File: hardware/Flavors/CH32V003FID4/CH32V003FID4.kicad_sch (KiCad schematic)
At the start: 22 parts, among them U1 TPS92520QDAPRQ1, U3 CH32V003F4P6

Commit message: Syncing the latest update on KiCAD (these updates are going to be randomly pushed i am not using Git for tracking it) and probably stuff will be without meaningfull commits. Commits are mainly for the code progress (and whatever that catches on KiCAD)
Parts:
- removed D1, D2: D_Shockley, Diode_SMD:D_SMA, symbol Device:D_Shockley
- added C12: 0.47u, Capacitor_SMD:C_1206_3216Metric, symbol Device:C_Small
- added C13: 47 µ, symbol Device:C_Polarized
- added D1, D2: 100V, symbol Device:D_Schottky
- added D3: SMBJ48A, symbol Device:D_TVS
- added J1: 48 POWER IN, symbol Connector:Screw_Terminal_01x02
- added L2: 150 u, symbol Device:L_Small
- added R4: 4.7K, symbol Device:R_Small
- added R5: 10K, symbol Device:R_Small
- added R6: 4.7 k (place holder), symbol Device:R_Small
- C10: value C_Small -> 100n
- C11: value C_Small -> 0.47u
- C4, C5: value C -> 1u
- C7, C8: value C_Small -> 2.2u
- C9: value C_Small -> 4.7u
- L1: value L_Small -> 150 u
- R1: value R_Small -> 10
- R2, R3: value R_Small -> 0.33
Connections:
- net +5V: now also C9.2, U1.9 (V5D), R4.1, R5.1; no longer C10.2, U1.8 (V5A)
- net GND: now also C10.2, C9.1, U1.33 (EP), C13.2, D1.2 (A), D2.2 (A), D3.1 (A1), J1.1 (Pin_1), R6.1; no longer C10.1, C9.2
- net VLED1: now also D2.1 (K)
- net VLED2: now also D1.1 (K)
- net at R2.1, U1.18 (CSP1): now also L2.1
- net at U1.19 (BST1): now also C12.1
- net at U1.20 (SW1): now also U1.21 (SW1), C12.2, L2.2
- net !FLT: now reaches U1.22 (FLT#)
- net !FLT: now also R5.2
- net at U1.23 (LHI): now also R6.2
- net SSN: now reaches U1.24 (SSN)
- net SCK: now reaches U1.25 (SCK)
- net MISO: now reaches U1.26 (MISO)
- net MISO: now also R4.2
- net MOSI: now reaches U1.27 (MOSI)
- net at C11.2, U1.28 (SW2), U1.29 (SW2): now also L1.2
- net at R3.1, U1.31 (CSP2): now also L1.1
- net VBOOST renamed +48V
- net +48V: now also C13.1, D3.2 (A2), J1.2 (Pin_2)
- new net: C10.1, R1.1, U1.8 (V5A)
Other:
- note added: "Inputs"
- moved on the sheet: C10, C5, L1

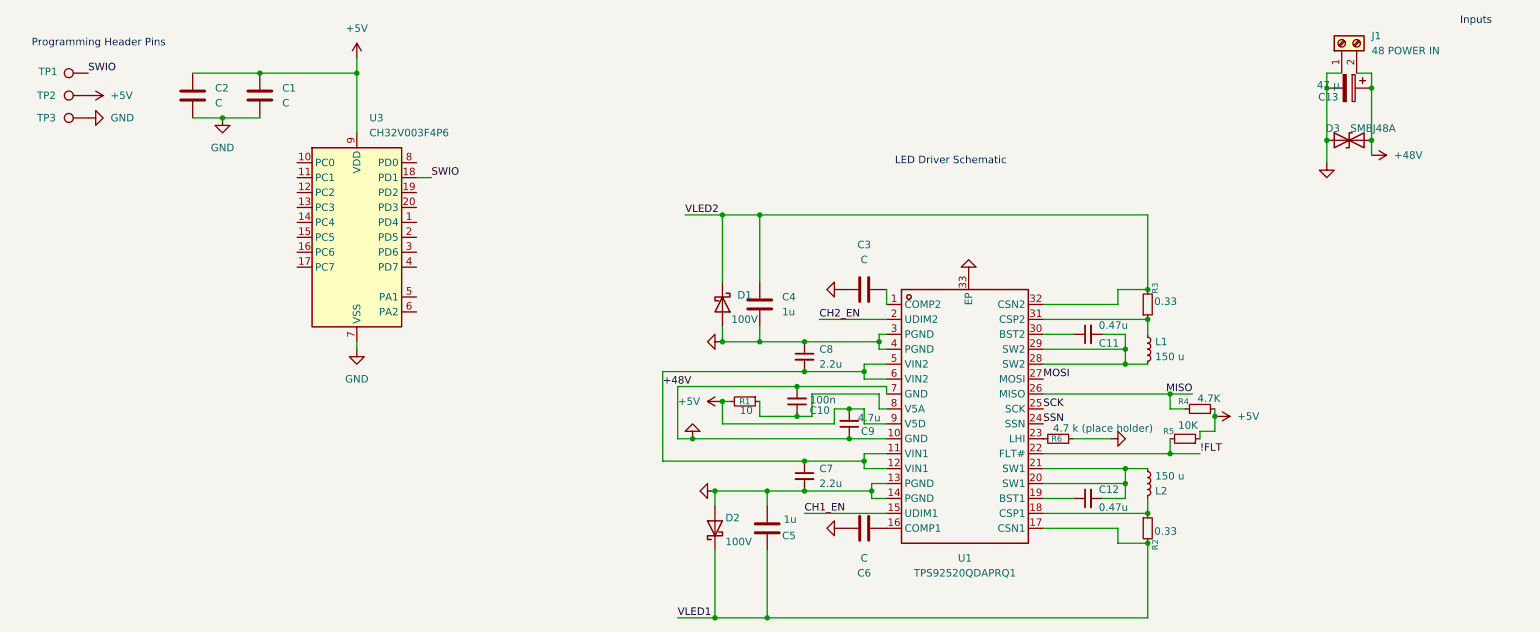
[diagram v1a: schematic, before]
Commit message: Removed debugging on overflow
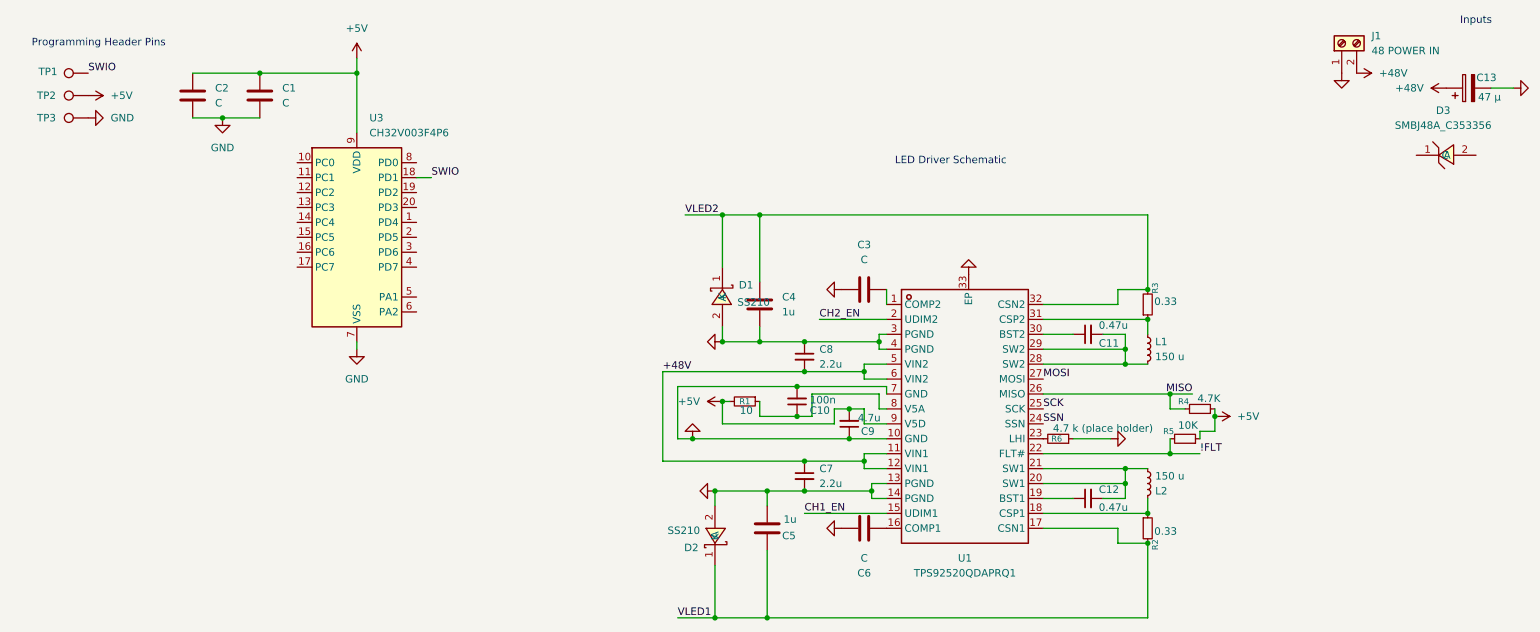
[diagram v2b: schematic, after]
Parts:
- removed D1, D2: 100V, symbol Device:D_Schottky
- removed D3: SMBJ48A, symbol Device:D_TVS
- added D1, D2: SS210, LCSC_Components:SMA_L4.3-W2.6-LS5.2-RD, symbol ModbusFID4:SS210
- added D3: SMBJ48A_C353356, SMBJ48A:SMB_L4.6-W3.6-LS5.3-RD, symbol ModbusFID4:SMBJ48A_C353356
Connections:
- net GND: now also D1.2 (A), D2.2 (A)
- net VLED1: now also D2.1 (K)
- net VLED2: now also D1.1 (K)
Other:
- moved on the sheet: C13
